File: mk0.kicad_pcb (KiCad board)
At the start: 2 copper layers, 94 parts, among them J1 USB_C_Receptacle_USB2.0_16P, J2 AudioJack4, J3 Conn_ARM_JTAG_SWD_10, SW1 SW_RESET, SW10 tab, SW11 q, SW12 w, SW13 e, SW14 r, SW15 t, SW16 [, SW17 caps, SW18 a, SW19 s, SW2 SW_BOOT, SW20 d, SW21 f, SW22 g, SW23 ->, SW24 shift, SW25 z, SW26 x, SW27 c, SW28 v, SW29 b, SW3 `, SW30 custom2, SW31 ctrl, SW32 menu, SW33 alt, SW34 space, SW35 custom1, SW36 custom3, SW4 1, SW5 2, SW6 3, SW7 4, SW8 5, SW9 -, U1 LM3480-3.3, U2 STM32F072CBTx, Y1 8MHz

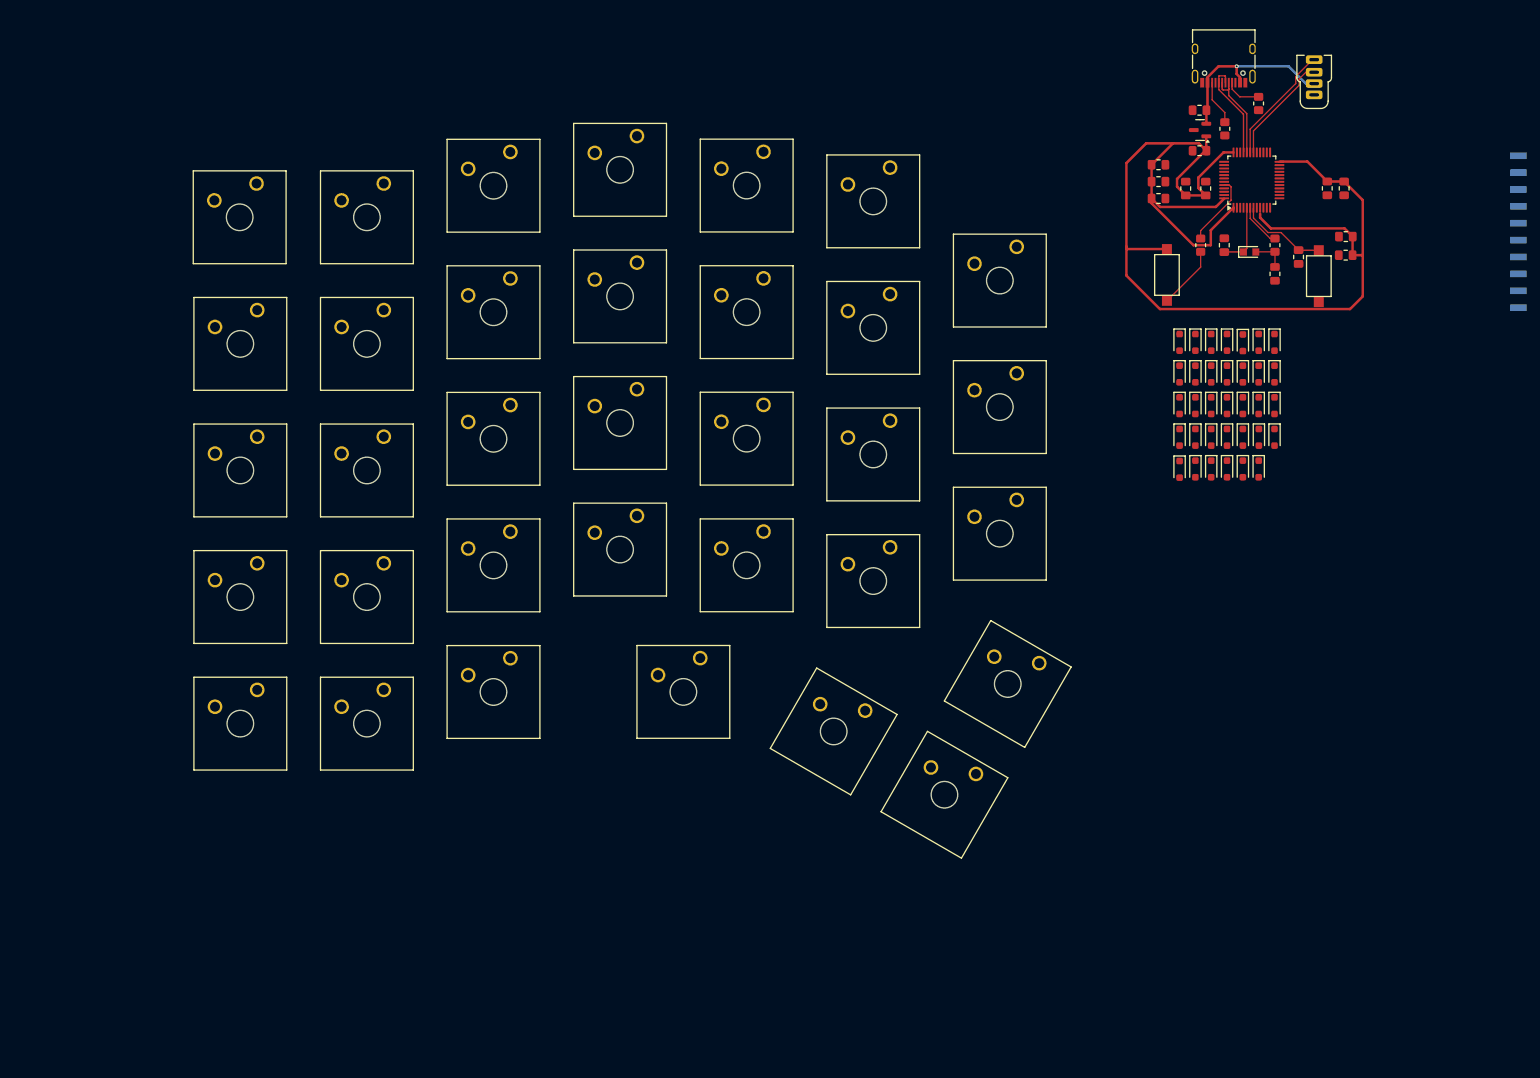
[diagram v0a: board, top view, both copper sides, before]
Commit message: Finish routing for switches
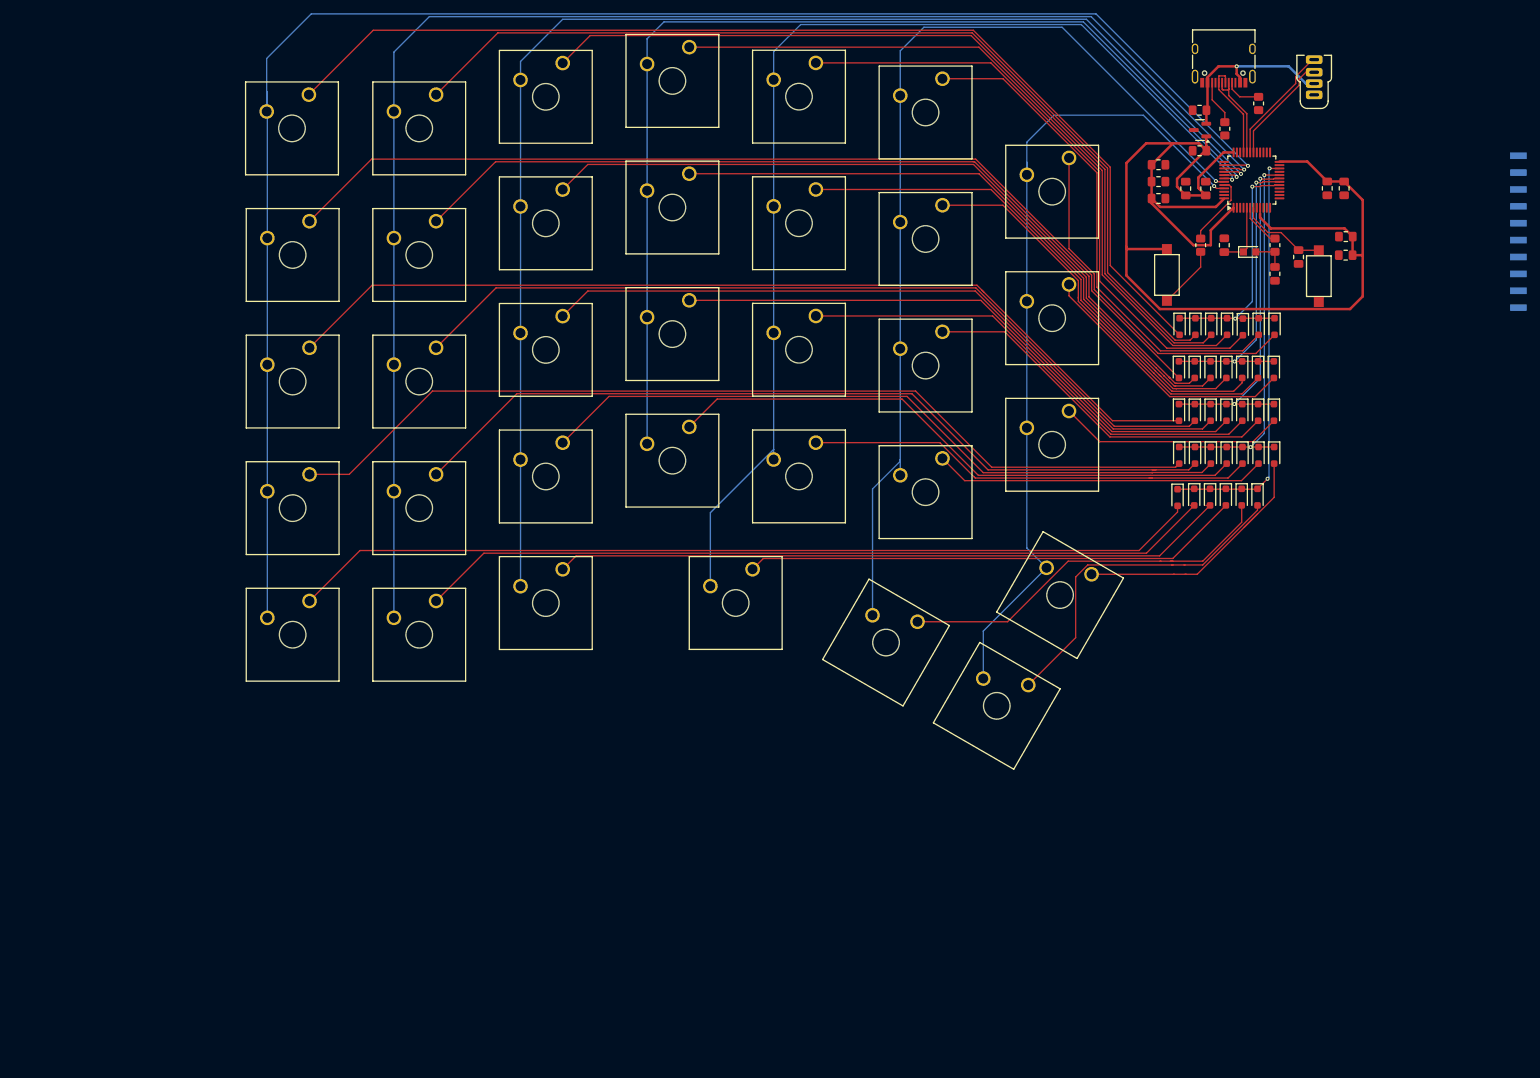
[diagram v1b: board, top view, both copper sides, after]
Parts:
- moved SW14 15.5 mm to (177.8, 38.9)
- moved SW21 15.5 mm to (177.8, 57.9)
- moved SW28 15.5 mm to (177.8, 77.0)
- moved SW30 15.5 mm to (219.3, 96.8)
- moved SW4 15.5 mm to (120.7, 24.6)
- moved SW7 15.5 mm to (177.8, 19.8)
- moved SW11 15.5 mm to (120.7, 43.6)
- moved SW18 15.5 mm to (120.7, 62.7)
- moved SW25 15.5 mm to (120.7, 81.7)
- moved SW32 15.5 mm to (120.7, 100.8)
- moved SW3 15.5 mm to (101.5, 24.6)
- moved SW5 15.5 mm to (139.7, 19.8)
- moved SW6 15.5 mm to (158.8, 17.4)
- moved SW10 15.5 mm to (101.6, 43.6)
- moved SW12 15.5 mm to (139.7, 38.9)
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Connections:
- U2 pad 17: unconnected-(U2-PA7-Pad17) -> Row0
- U2 pad 18: Row0 -> Row1
- U2 pad 19: Row1 -> Row2
- U2 pad 20: Row2 -> Row3
- U2 pad 21: Col6 -> unconnected-(U2-PB10-Pad21)
- U2 pad 22: Row3 -> Row4
- U2 pad 25: Row4 -> unconnected-(U2-PB12-Pad25)
- U2 pad 42: unconnected-(U2-PB6-Pad42) -> Col4
- U2 pad 43: unconnected-(U2-PB7-Pad43) -> Col5
- U2 pad 45: Col4 -> Col6
- U2 pad 46: Col5 -> unconnected-(U2-PB9-Pad46)
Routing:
- net Col0: track 0.00 -> 250.8 mm, vias 0 -> 1
- net Col1: track 0.00 -> 227.9 mm, vias 0 -> 1
- net Col2: track 0.00 -> 202.3 mm, vias 0 -> 1
- net Col4: track 0.00 -> 167.9 mm, vias 0 -> 1
- net Net-(D1-A): track 0.00 -> 162.7 mm
- net Col3: track 0.00 -> 162.5 mm, vias 0 -> 1
- net Net-(D8-A): track 0.00 -> 149.7 mm
- net Col5: track 0.00 -> 148.9 mm, vias 0 -> 1
- net Net-(D2-A): track 0.00 -> 146.8 mm
- net Net-(D15-A): track 0.00 -> 143.5 mm
- net Net-(D22-A): track 0.00 -> 141.0 mm
- net Net-(D29-A): track 0.00 -> 137.4 mm
- net Net-(D9-A): track 0.00 -> 134.2 mm
- net Net-(D3-A): track 0.00 -> 128.2 mm
- net Net-(D16-A): track 0.00 -> 126.9 mm
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
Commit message: Complete left halve
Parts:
- moved J3 84.5 mm to (228.7, 104.3)
- moved C7 45.4 mm to (232.3, 76.6)
- moved C11 45.4 mm to (204.4, 78.2)
- moved C13 45.4 mm to (214.3, 85.2)
- moved C14 45.4 mm to (221.9, 89.5)
- moved C3 45.4 mm to (210.6, 71.0)
- moved C4 45.4 mm to (210.6, 64.9)
- moved C8 45.4 mm to (229.8, 76.6)
- moved D10 45.4 mm to (212.2, 103.9)
- moved D11 45.4 mm to (214.6, 103.9)
- moved D12 45.4 mm to (217.0, 103.9)
- moved D13 45.4 mm to (219.4, 103.9)
- moved D14 45.4 mm to (221.7, 103.9)
- moved D29 45.4 mm to (207.3, 123.2)
- moved D30 45.4 mm to (209.8, 123.1)
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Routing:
- net GND: track 0.16 -> 110.8 mm, vias 0 -> 10
- net SWDIO: track 0.00 -> 59.6 mm, vias 0 -> 1
- net 3.3V: track 190.5 -> 215.9 mm, vias 0 -> 1
- net SWDCLK: track 0.00 -> 5.44 mm, vias 0 -> 1
- net Net-(D28-A): track 40.5 -> 37.7 mm
- net unconnected-(J3-NC/TDI-Pad8): track 0.00 -> 2.64 mm
- net RESET: track 13.4 -> 15.5 mm, vias 0 -> 1
- net Net-(D34-A): track 51.8 -> 53.5 mm
- net Net-(D31-A): track 102.3 -> 101.7 mm
- net Net-(D30-A): track 121.0 -> 120.3 mm
- net Net-(D23-A): track 124.9 -> 124.4 mm
- added copper zone on B.Cu, net GND
- added copper zone on F.Cu, net GND
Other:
- board outline added: 171.7 x 116.9 mm
